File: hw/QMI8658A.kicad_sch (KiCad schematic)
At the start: 3 parts, among them U6 QMI8658A

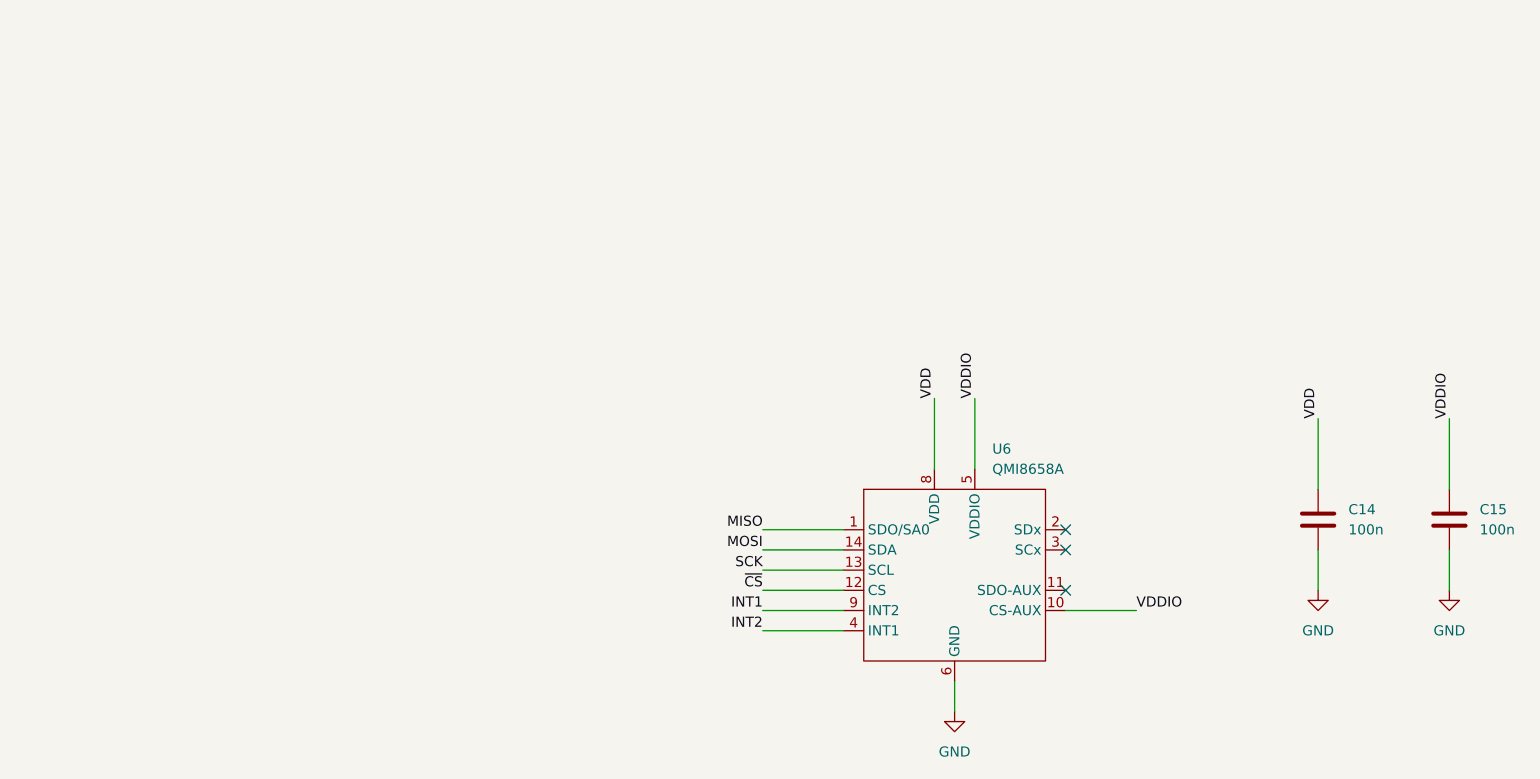
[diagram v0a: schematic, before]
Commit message: updated and fix ERCs
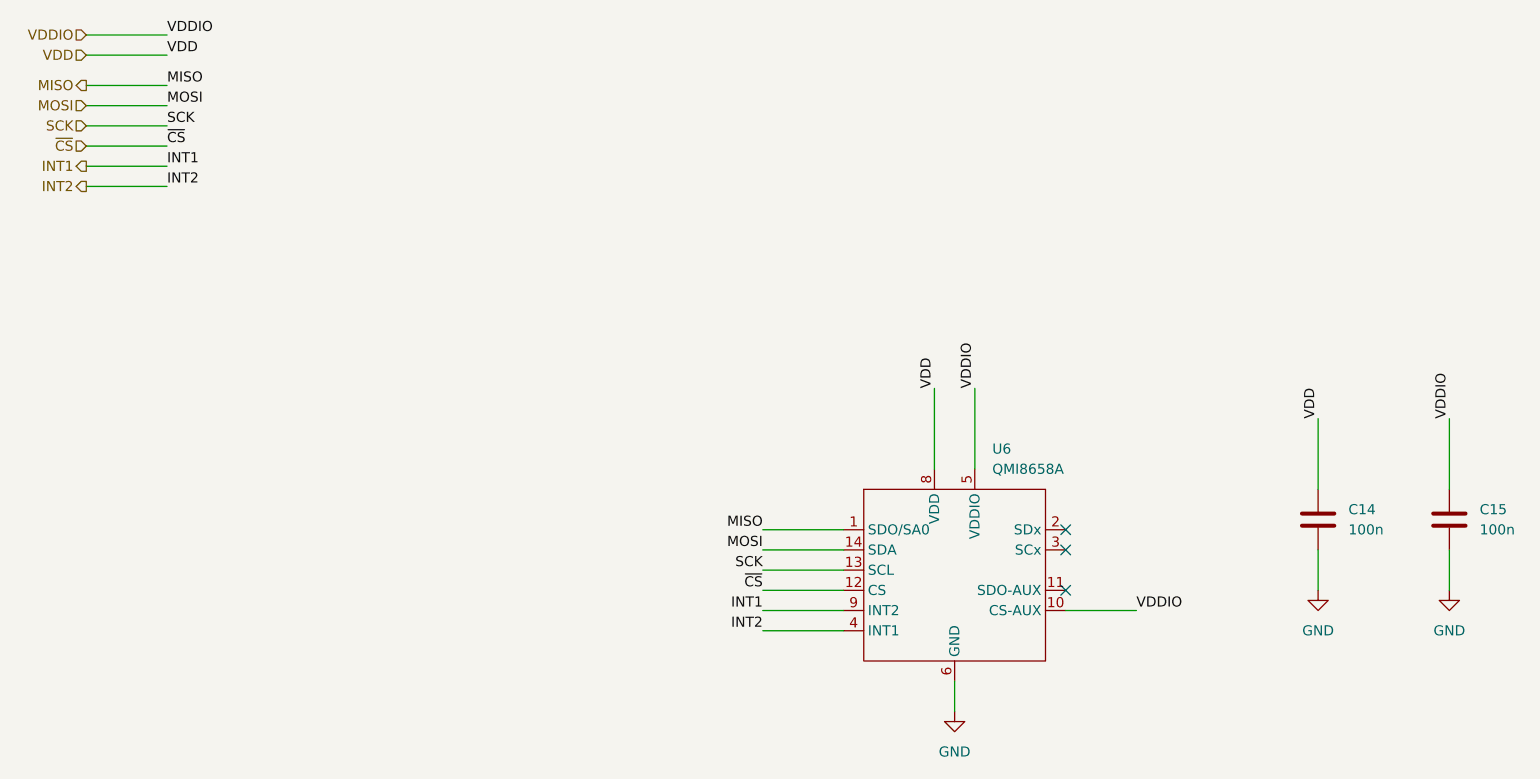
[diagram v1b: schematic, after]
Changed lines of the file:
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@@
   (no_connect (at 162.56 95.25))
   (no_connect (at 162.56 92.71))
-  (wire (pts (xy 146.05 76.2) (xy 146.05 85.09))
+  (wire (pts (xy 39.37 36.83) (xy 49.53 36.83))
+    (stroke (width 0) (type default))
+  )
+  (wire (pts (xy 146.05 74.93) (xy 146.05 85.09))
+    (stroke (width 0) (type default))
+  )
+  (wire (pts (xy 39.37 44.45) (xy 49.53 44.45))
+    (stroke (width 0) (type default))
+  )
+  (wire (pts (xy 39.37 39.37) (xy 49.53 39.37))
     (stroke (width 0) (type default))
   )
@@
     (stroke (width 0) (type default))
   )
-  (wire (pts (xy 151.13 76.2) (xy 151.13 85.09))
+  (wire (pts (xy 151.13 74.93) (xy 151.13 85.09))
     (stroke (width 0) (type default))
   )
@@
     (stroke (width 0) (type default))
   )
+  (wire (pts (xy 39.37 33.02) (xy 49.53 33.02))
+    (stroke (width 0) (type default))
+  )
+  (wire (pts (xy 39.37 41.91) (xy 49.53 41.91))
+    (stroke (width 0) (type default))
+  )
   (wire (pts (xy 194.31 95.25) (xy 194.31 100.33))
     (stroke (width 0) (type default))
@@
     (stroke (width 0) (type default))
   )
+  (wire (pts (xy 39.37 46.99) (xy 49.53 46.99))
+    (stroke (width 0) (type default))
+  )
   (wire (pts (xy 124.46 102.87) (xy 134.62 102.87))
     (stroke (width 0) (type default))
   )
+  (wire (pts (xy 39.37 30.48) (xy 49.53 30.48))
+    (stroke (width 0) (type default))
+  )
   (wire (pts (xy 171.45 102.87) (xy 162.56 102.87))
+    (stroke (width 0) (type default))
+  )
+  (wire (pts (xy 39.37 49.53) (xy 49.53 49.53))
     (stroke (width 0) (type default))
   )
@@
     (effects (font (size 1.27 1.27)) (justify right bottom))
   )
+  (label "INT2" (at 49.53 49.53 0) (fields_autoplaced)
+    (effects (font (size 1.27 1.27)) (justify left bottom))
+  )
   (label "SCK" (at 124.46 97.79 180) (fields_autoplaced)
     (effects (font (size 1.27 1.27)) (justify right bottom))
@@
     (effects (font (size 1.27 1.27)) (justify right bottom))
   )
-  (label "VDDIO" (at 151.13 76.2 90) (fields_autoplaced)
+  (label "VDDIO" (at 151.13 74.93 90) (fields_autoplaced)
     (effects (font (size 1.27 1.27)) (justify left bottom))
   )
-  (label "VDD" (at 146.05 76.2 90) (fields_autoplaced)
+  (label "VDDIO" (at 49.53 30.48 0) (fields_autoplaced)
+    (effects (font (size 1.27 1.27)) (justify left bottom))
+  )
+  (label "VDD" (at 146.05 74.93 90) (fields_autoplaced)
+    (effects (font (size 1.27 1.27)) (justify left bottom))
+  )
+  (label "MOSI" (at 49.53 39.37 0) (fields_autoplaced)
     (effects (font (size 1.27 1.27)) (justify left bottom))
   )
@@
     (effects (font (size 1.27 1.27)) (justify right bottom))
   )
+  (label "VDD" (at 49.53 33.02 0) (fields_autoplaced)
+    (effects (font (size 1.27 1.27)) (justify left bottom))
+  )
+  (label "MISO" (at 49.53 36.83 0) (fields_autoplaced)
+    (effects (font (size 1.27 1.27)) (justify left bottom))
+  )
+  (label "~{CS}" (at 49.53 44.45 0) (fields_autoplaced)
+    (effects (font (size 1.27 1.27)) (justify left bottom))
+  )
   (label "VDDIO" (at 171.45 102.87 0) (fields_autoplaced)
+    (effects (font (size 1.27 1.27)) (justify left bottom))
+  )
+  (label "SCK" (at 49.53 41.91 0) (fields_autoplaced)
+    (effects (font (size 1.27 1.27)) (justify left bottom))
+  )
+  (label "INT1" (at 49.53 46.99 0) (fields_autoplaced)
     (effects (font (size 1.27 1.27)) (justify left bottom))
   )
@@
     (effects (font (size 1.27 1.27)) (justify right bottom))
   )
+  (hierarchical_label "MISO" (shape output) (at 39.37 36.83 180) (fields_autoplaced)
+    (effects (font (size 1.27 1.27)) (justify right))
+  )
+  (hierarchical_label "MOSI" (shape input) (at 39.37 39.37 180) (fields_autoplaced)
+    (effects (font (size 1.27 1.27)) (justify right))
+  )
+  (hierarchical_label "SCK" (shape input) (at 39.37 41.91 180) (fields_autoplaced)
+    (effects (font (size 1.27 1.27)) (justify right))
+  )
+  (hierarchical_label "VDD" (shape input) (at 39.37 33.02 180) (fields_autoplaced)
+    (effects (font (size 1.27 1.27)) (justify right))
+  )
+  (hierarchical_label "VDDIO" (shape input) (at 39.37 30.48 180) (fields_autoplaced)
+    (effects (font (size 1.27 1.27)) (justify right))
+  )
+  (hierarchical_label "~{CS}" (shape input) (at 39.37 44.45 180) (fields_autoplaced)
+    (effects (font (size 1.27 1.27)) (justify right))
+  )
+  (hierarchical_label "INT1" (shape output) (at 39.37 46.99 180) (fields_autoplaced)
+    (effects (font (size 1.27 1.27)) (justify right))
+  )
+  (hierarchical_label "INT2" (shape output) (at 39.37 49.53 180) (fields_autoplaced)
+    (effects (font (size 1.27 1.27)) (justify right))
+  )
   (symbol (lib_id "power:GND") (at 210.82 100.33 0) (unit 1)

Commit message: fix DRCs
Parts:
- U6: footprint Package_LGA:LGA-14_3x2.5mm_P0.5mm_LayoutBorder3x4y -> IotPi_Package_LGA:LGA-14_3x2.5mm_P0.5mm_LayoutBorder3x4y
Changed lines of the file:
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@@
       (effects (font (size 1.27 1.27)) (justify left))
     )
-    (property "Footprint" "Package_LGA:LGA-14_3x2.5mm_P0.5mm_LayoutBorder3x4y" (at 149.86 124.46 0)
+    (property "Footprint" "IotPi_Package_LGA:LGA-14_3x2.5mm_P0.5mm_LayoutBorder3x4y" (at 149.86 124.46 0)
       (effects (font (size 1.27 1.27)) hide)
     )

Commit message: updated sheets information
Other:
- company: (none) -> Qingdao IotPi Information Technology Ltd.,
- title: (none) -> KiCad 2023 Shen Zhen Badge
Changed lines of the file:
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@@
 (kicad_sch (version 20230121) (generator eeschema)
   (paper "A4")
+  (title_block
+    (title "KiCad 2023 Shen Zhen Badge")
+    (date "2023-09-04")
+    (rev "1")
+    (company "Qingdao IotPi Information Technology Ltd.,")
+    (comment 1 "Designed by Yang Hongbo")
+  )
   (no_connect (at 162.56 100.33))
   (no_connect (at 162.56 95.25))
